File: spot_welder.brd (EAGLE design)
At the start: 77 x 53.8 mm, 38 parts, among them IC1 ATMEGA328PU, IC2 7805L, IC3 MOC3052M, T1 BT151-800R, T2 BT151-800R, Y1 16MHZ

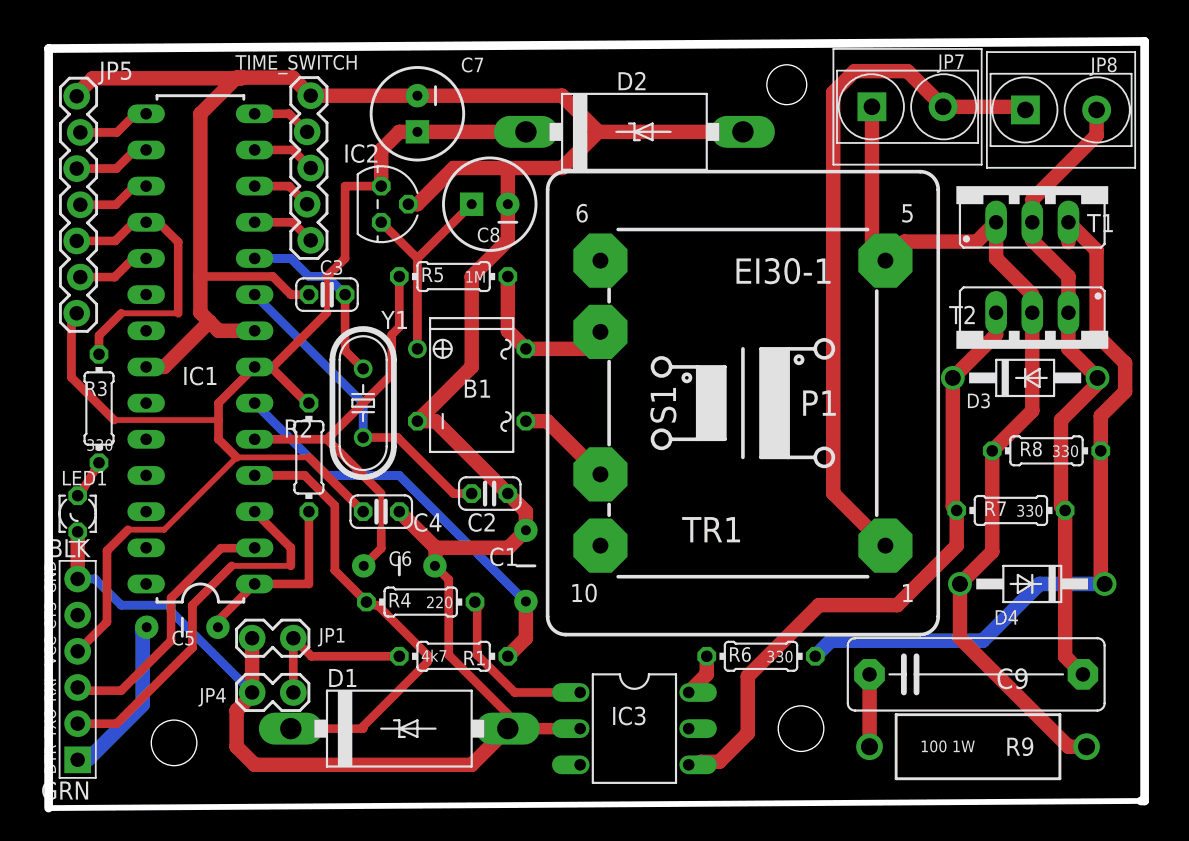
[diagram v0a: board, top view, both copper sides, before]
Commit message: added VCC & GND planes
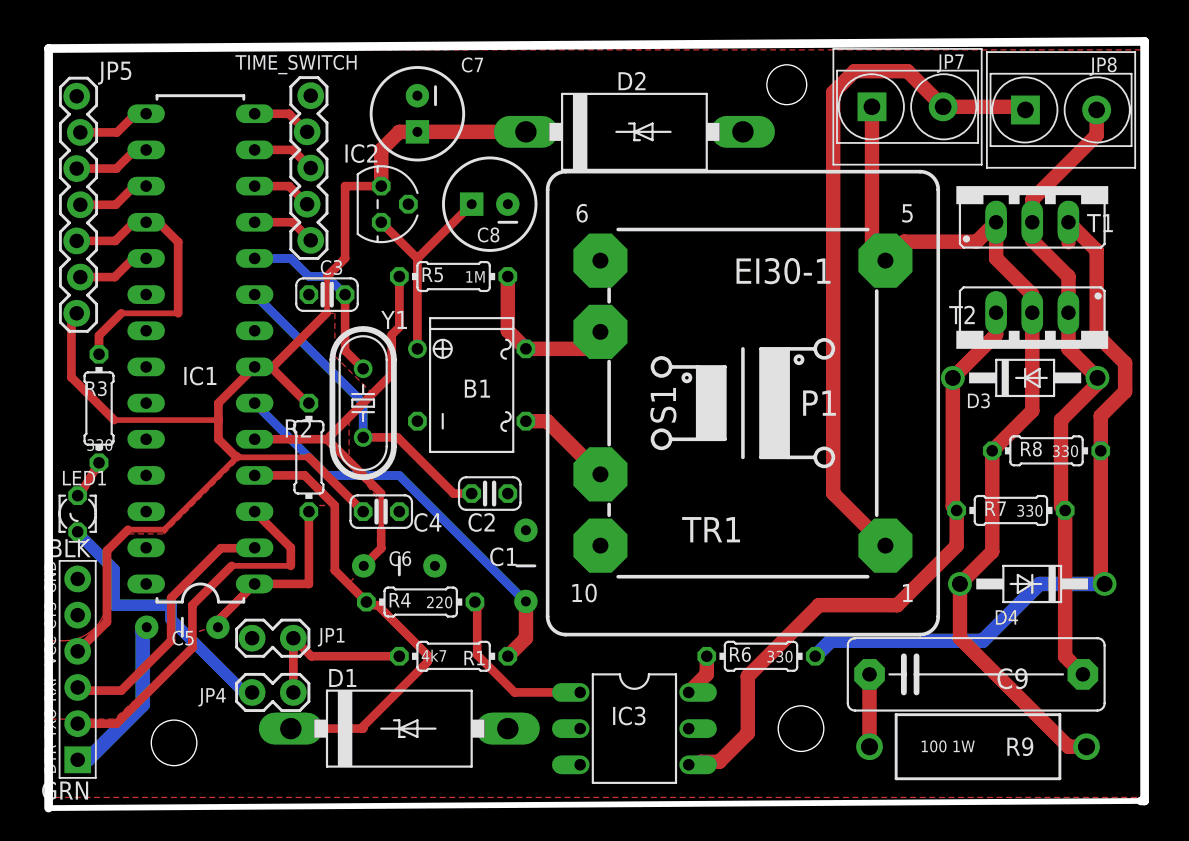
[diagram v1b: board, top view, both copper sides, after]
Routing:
- net GND: track 210.8 -> 19.2 mm
- added copper zone on layer 1, net GND
- added copper zone on layer 1, net VCC
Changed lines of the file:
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@@
 <contactref element="TIME_SWITCH" pad="1"/>
 <contactref element="JP4" pad="1"/>
-<wire x1="58.38" y1="50.8" x2="58.42" y2="50.76" width="0.6096" layer="1"/>
-<wire x1="43.18" y1="67.31" x2="41.91" y2="67.31" width="0.6096" layer="1"/>
-<wire x1="41.91" y1="67.31" x2="40.64" y2="68.58" width="0.6096" layer="1"/>
-<wire x1="40.64" y1="68.58" x2="35.56" y2="68.58" width="0.6096" layer="1"/>
 <wire x1="39.1922" y1="39.37" x2="39.1922" y2="39.1922" width="0.6096" layer="1"/>
-<wire x1="50.165" y1="73.66" x2="50.8" y2="73.66" width="1.016" layer="1"/>
-<wire x1="50.8" y1="73.66" x2="53.34" y2="76.2" width="1.016" layer="1"/>
-<wire x1="53.34" y1="76.2" x2="57.15" y2="76.2" width="1.016" layer="1"/>
-<wire x1="57.15" y1="76.2" x2="60.96" y2="76.2" width="1.016" layer="1"/>
-<wire x1="60.96" y1="76.2" x2="63.5" y2="78.74" width="1.016" layer="1"/>
-<wire x1="63.5" y1="78.74" x2="73.66" y2="78.74" width="1.016" layer="1"/>
-<wire x1="50.8" y1="81.28" x2="60.96" y2="81.28" width="1.016" layer="1"/>
-<wire x1="60.96" y1="81.28" x2="63.5" y2="78.74" width="1.016" layer="1"/>
-<wire x1="50.8" y1="81.28" x2="43.307" y2="81.28" width="1.016" layer="1"/>
-<wire x1="36.83" y1="64.77" x2="36.195" y2="65.405" width="1.016" layer="1"/>
-<wire x1="36.195" y1="65.405" x2="35.56" y2="66.04" width="1.016" layer="1"/>
-<wire x1="35.56" y1="66.04" x2="35.56" y2="68.58" width="1.016" layer="1"/>
-<wire x1="35.56" y1="68.58" x2="35.56" y2="80.01" width="1.016" layer="1"/>
-<wire x1="35.56" y1="80.01" x2="38.1" y2="82.55" width="1.016" layer="1"/>
-<wire x1="38.1" y1="82.55" x2="38.5" y2="82.55" width="1.016" layer="1"/>
-<wire x1="38.5" y1="82.55" x2="42.037" y2="82.55" width="1.016" layer="1"/>
-<wire x1="42.037" y1="82.55" x2="43.307" y2="81.28" width="1.016" layer="1"/>
-<wire x1="33.02" y1="62.23" x2="36.195" y2="65.405" width="1.016" layer="1"/>
-<wire x1="57.15" y1="73.66" x2="57.15" y2="76.2" width="1.016" layer="1"/>
-<wire x1="50.8" y1="58.42" x2="54.61" y2="62.23" width="1.016" layer="1"/>
-<wire x1="54.61" y1="62.23" x2="54.61" y2="68.58" width="1.016" layer="1"/>
-<wire x1="54.61" y1="68.58" x2="57.15" y2="71.12" width="1.016" layer="1"/>
-<wire x1="57.15" y1="71.12" x2="57.15" y2="73.66" width="1.016" layer="1"/>
-<wire x1="57.15" y1="53.34" x2="58.42" y2="52.07" width="1.016" layer="1"/>
-<wire x1="58.42" y1="52.07" x2="58.42" y2="50.76" width="1.016" layer="1"/>
-<wire x1="39.1922" y1="43.18" x2="39.1922" y2="39.37" width="1.016" layer="1"/>
-<wire x1="39.1922" y1="39.1922" x2="38.1" y2="38.1" width="1.016" layer="1"/>
-<wire x1="38.1" y1="38.1" x2="38.1" y2="35.56" width="1.016" layer="1"/>
-<wire x1="38.1" y1="35.56" x2="39.37" y2="34.29" width="1.016" layer="1"/>
-<wire x1="39.37" y1="34.29" x2="54.61" y2="34.29" width="1.016" layer="1"/>
-<wire x1="54.61" y1="34.29" x2="57.15" y2="36.83" width="1.016" layer="1"/>
-<wire x1="52.07" y1="49.53" x2="57.19" y2="49.53" width="1.016" layer="1"/>
-<wire x1="57.19" y1="49.53" x2="58.42" y2="50.76" width="1.016" layer="1"/>
-<wire x1="52.07" y1="49.53" x2="52.07" y2="48.3" width="1.016" layer="1"/>
-<wire x1="52.07" y1="48.3" x2="52.03" y2="48.26" width="1.016" layer="1"/>
-<wire x1="50.8" y1="58.42" x2="52.07" y2="58.42" width="1.016" layer="1"/>
-<wire x1="52.07" y1="58.42" x2="57.15" y2="53.34" width="1.016" layer="1"/>
-<wire x1="26.94" y1="47.34" x2="26.94" y2="50.65" width="1.016" layer="1"/>
 <contactref element="JP5" pad="7"/>
 <contactref element="IC1" pad="8"/>
 <contactref element="C4" pad="1"/>
 <contactref element="IC1" pad="22"/>
-<wire x1="57.15" y1="36.83" x2="62.23" y2="36.83" width="0.8128" layer="1"/>
-<wire x1="36.83" y1="64.77" x2="39.37" y2="64.77" width="1.016" layer="1"/>
-<wire x1="26.873" y1="81.24" x2="26.873" y2="81.373" width="1.016" layer="1"/>
-<wire x1="26.873" y1="81.373" x2="28" y2="82.5" width="1.016" layer="1"/>
-<wire x1="28" y1="82.5" x2="38.45" y2="82.5" width="1.016" layer="1"/>
-<wire x1="38.45" y1="82.5" x2="38.5" y2="82.55" width="1.016" layer="1"/>
-<wire x1="33.02" y1="62.23" x2="31.75" y2="62.23" width="1.016" layer="1"/>
-<wire x1="49.53" y1="52.07" x2="52.07" y2="49.53" width="1.016" layer="1"/>
-<wire x1="57.15" y1="36.83" x2="57.15" y2="37.85" width="0.6096" layer="1"/>
-<wire x1="57.15" y1="37.85" x2="53" y2="42" width="0.6096" layer="1"/>
-<wire x1="53" y1="42" x2="53" y2="47.29" width="0.6096" layer="1"/>
-<wire x1="53" y1="47.29" x2="52.03" y2="48.26" width="0.6096" layer="1"/>
-<wire x1="26.94" y1="47.34" x2="28.16" y2="47.34" width="0.6096" layer="16"/>
-<wire x1="28.16" y1="47.34" x2="30" y2="45.5" width="0.6096" layer="16"/>
-<wire x1="30" y1="45.5" x2="33.5" y2="45.5" width="0.6096" layer="16"/>
-<wire x1="33.5" y1="45.5" x2="33.5" y2="45.0622" width="0.6096" layer="16"/>
-<wire x1="33.5" y1="45.0622" x2="39.1922" y2="39.37" width="0.6096" layer="16"/>
+<wire x1="26.94" y1="50.65" x2="26.94" y2="50.56" width="0.8128" layer="16"/>
+<wire x1="26.94" y1="50.56" x2="29.5" y2="48" width="0.8128" layer="16"/>
+<wire x1="29.5" y1="48" x2="29.5" y2="45.5" width="0.8128" layer="16"/>
+<wire x1="29.5" y1="45.5" x2="33.5" y2="45.5" width="0.8128" layer="16"/>
+<wire x1="33.5" y1="45.5" x2="33.5" y2="44.5" width="0.8128" layer="16"/>
+<wire x1="33.5" y1="44.5" x2="38.5" y2="39.5" width="0.8128" layer="16"/>
+<wire x1="38.5" y1="39.5" x2="39.0622" y2="39.5" width="0.8128" layer="16"/>
+<wire x1="39.0622" y1="39.5" x2="39.1922" y2="39.37" width="0.8128" layer="16"/>
+<polygon width="0.4064" layer="1" isolate="0.3048" thermals="no">
+<vertex x="25" y="84.5"/>
+<vertex x="102" y="84.5"/>
+<vertex x="102" y="32"/>
+<vertex x="25" y="32"/>
+</polygon>
 </signal>
 <signal name="VCC">
@@
 <wire x1="29" y1="49.32" x2="29" y2="44.32" width="0.6096" layer="1"/>
 <wire x1="29" y1="44.32" x2="26.94" y2="42.26" width="0.6096" layer="1"/>
+<polygon width="0.4064" layer="1" isolate="0.3048" thermals="no">
+<vertex x="25" y="43"/>
+<vertex x="26" y="43" curve="90"/>
+<vertex x="29" y="46"/>
+<vertex x="29" y="49"/>
+<vertex x="30.5" y="50.5"/>
+<vertex x="33" y="50.5"/>
+<vertex x="38.5" y="56"/>
+<vertex x="37" y="57"/>
+<vertex x="37" y="60"/>
+<vertex x="39.5" y="62.5"/>
+<vertex x="41" y="62.5"/>
+<vertex x="44.5" y="66"/>
+<vertex x="45" y="66"/>
+<vertex x="45" y="63"/>
+<vertex x="47.5" y="60.5"/>
+<vertex x="46" y="58.5"/>
+<vertex x="46" y="55.5"/>
+<vertex x="48" y="53"/>
+<vertex x="48" y="49.5"/>
+<vertex x="46" y="47"/>
+<vertex x="45" y="48"/>
+<vertex x="45" y="52.5"/>
+<vertex x="43.5" y="52.5"/>
+<vertex x="43" y="51.5"/>
+<vertex x="43" y="47"/>
+<vertex x="39.5" y="47"/>
+<vertex x="36.5" y="44"/>
+<vertex x="35" y="43.5"/>
+<vertex x="35" y="42.5"/>
+<vertex x="29.5" y="37.5"/>
+<vertex x="25" y="37.5"/>
+</polygon>
 </signal>
 <signal name="N$3">

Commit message: rerouted
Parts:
- removed TIME_SWITCH: Time switch, SparkFun-Connectors:1X05_LOCK
- added S5: Time switch, SparkFun-Connectors:1X05_NO_SILK
- C5, C6: device SparkFun-Passives:CAP-PTH-5MM -> rcl:C025-024X044
- JP5: device SparkFun-Connectors:1X07_LOCK -> SparkFun-Connectors:1X07_NO_SILK
- moved C1 18.2 mm to (41.3, 42.1), turned to 0 degrees
- moved C4 18.1 mm to (49.8, 70.1)
- moved R1 17.7 mm to (35.8, 39.4)
- moved R5 15.3 mm to (50.3, 53.6)
- moved D1 14.8 mm to (57.2, 49.5), turned to 90 degrees
- moved JP2 14.2 mm to (40.5, 36.9), turned to 180 degrees
- moved C5 12.8 mm to (47.0, 42.8), turned to 90 degrees
- moved R2 12.2 mm to (39.6, 44.2), turned to 0 degrees
- moved JP1 11.0 mm to (31.2, 45.6), turned to 90 degrees
- moved JP4 6.26 mm to (33.6, 41.9), turned to 90 degrees
- moved C2 5.53 mm to (51.8, 57.1), turned to 90 degrees
- moved R9 5.42 mm to (90.8, 40.9), turned to 180 degrees
- moved JP5 4.03 mm to (31.0, 65.5)
- moved LED1 4.00 mm to (30.9, 51.9)
- moved C9 3.89 mm to (91.0, 36.9), turned to 180 degrees
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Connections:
- net GND: now also JP5.1, S5.5; no longer JP5.7, TIME_SWITCH.1
- net N$18: now also S5.4; no longer TIME_SWITCH.5
- net N$23: now also S5.3; no longer TIME_SWITCH.4
- net N$24: now also S5.2; no longer TIME_SWITCH.3
- net N$25: now also S5.1; no longer TIME_SWITCH.2
- net VCC: now also JP5.7; no longer JP5.1
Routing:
- net GND: track 19.2 -> 0.00 mm
- net N$13: track 29.6 -> 11.2 mm
- net N$10: track 66.2 -> 56.2 mm
- net N$1: track 11.3 -> 21.1 mm
- net N$15: track 32.1 -> 22.7 mm
- net N$3: track 45.1 -> 54.3 mm
- net N$19: track 26.2 -> 18.4 mm
- net N$7: track 11.7 -> 4.66 mm
- net N$14: track 13.0 -> 6.92 mm
- net N$16: track 22.4 -> 16.7 mm
- net N$22: track 29.2 -> 23.6 mm
- net N$2: track 15.3 -> 10.5 mm
- net N$20: track 18.4 -> 14.8 mm
- net VCC: track 89.9 -> 93.1 mm
- net N$6: track 45.9 -> 42.8 mm
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- removed copper zone on layer 1, net VCC
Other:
- board size 77 x 53.8 mm -> 75.5 x 51 mm
